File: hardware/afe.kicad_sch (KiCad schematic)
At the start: 27 parts, among them U2 MCP6002-xMC, U3 4052

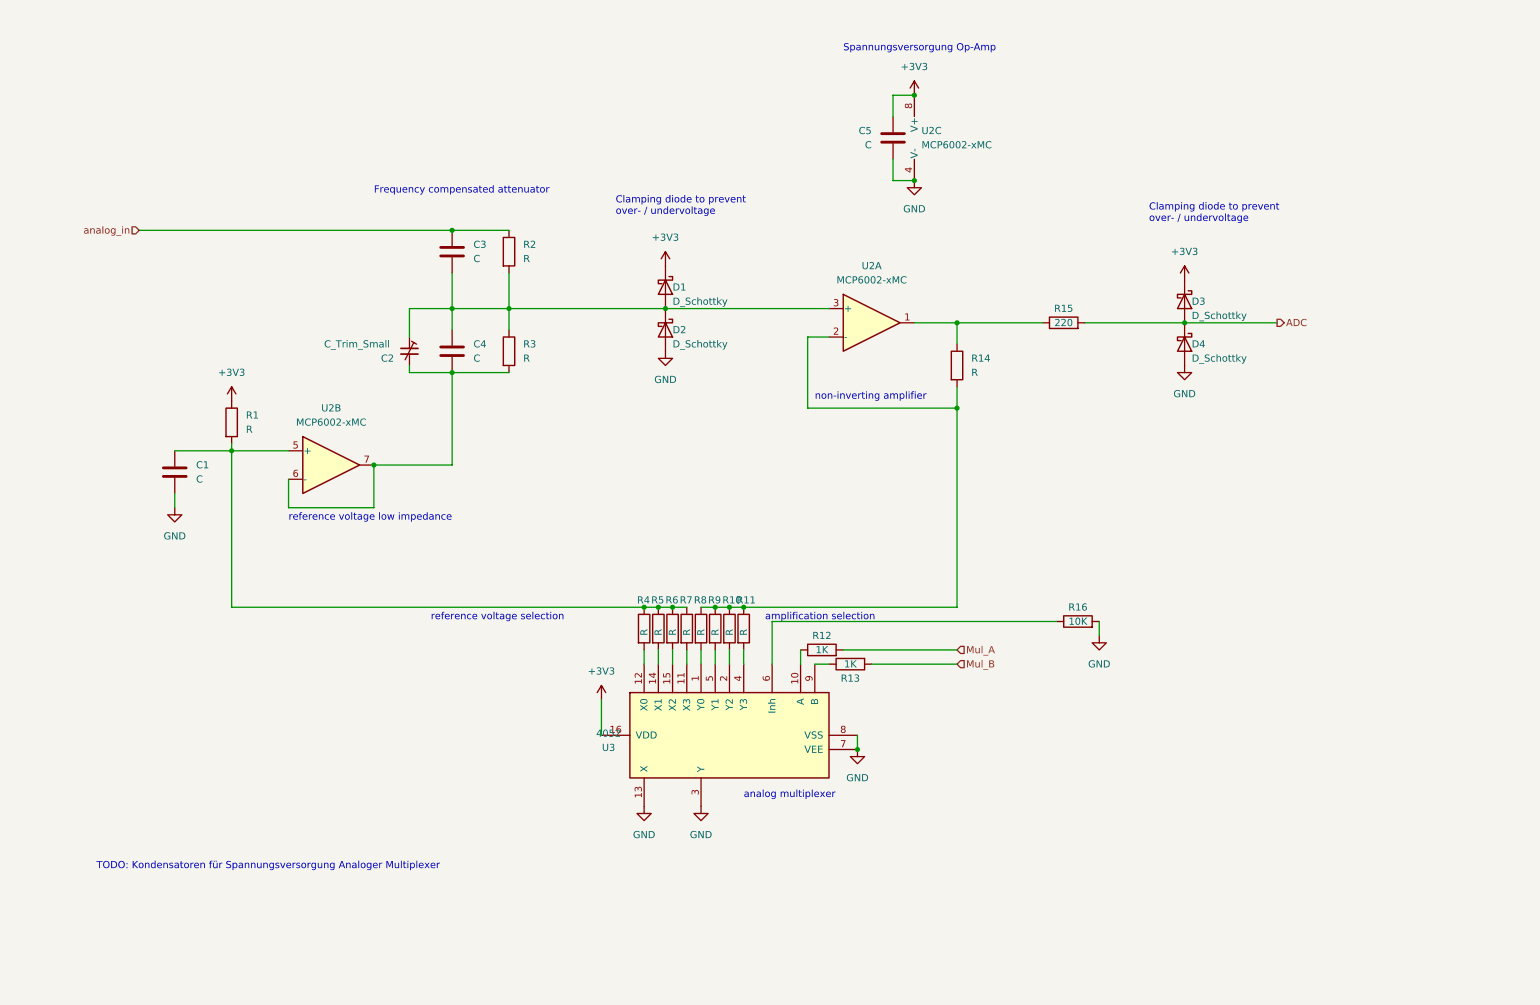
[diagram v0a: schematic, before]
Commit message: started adding some footprints
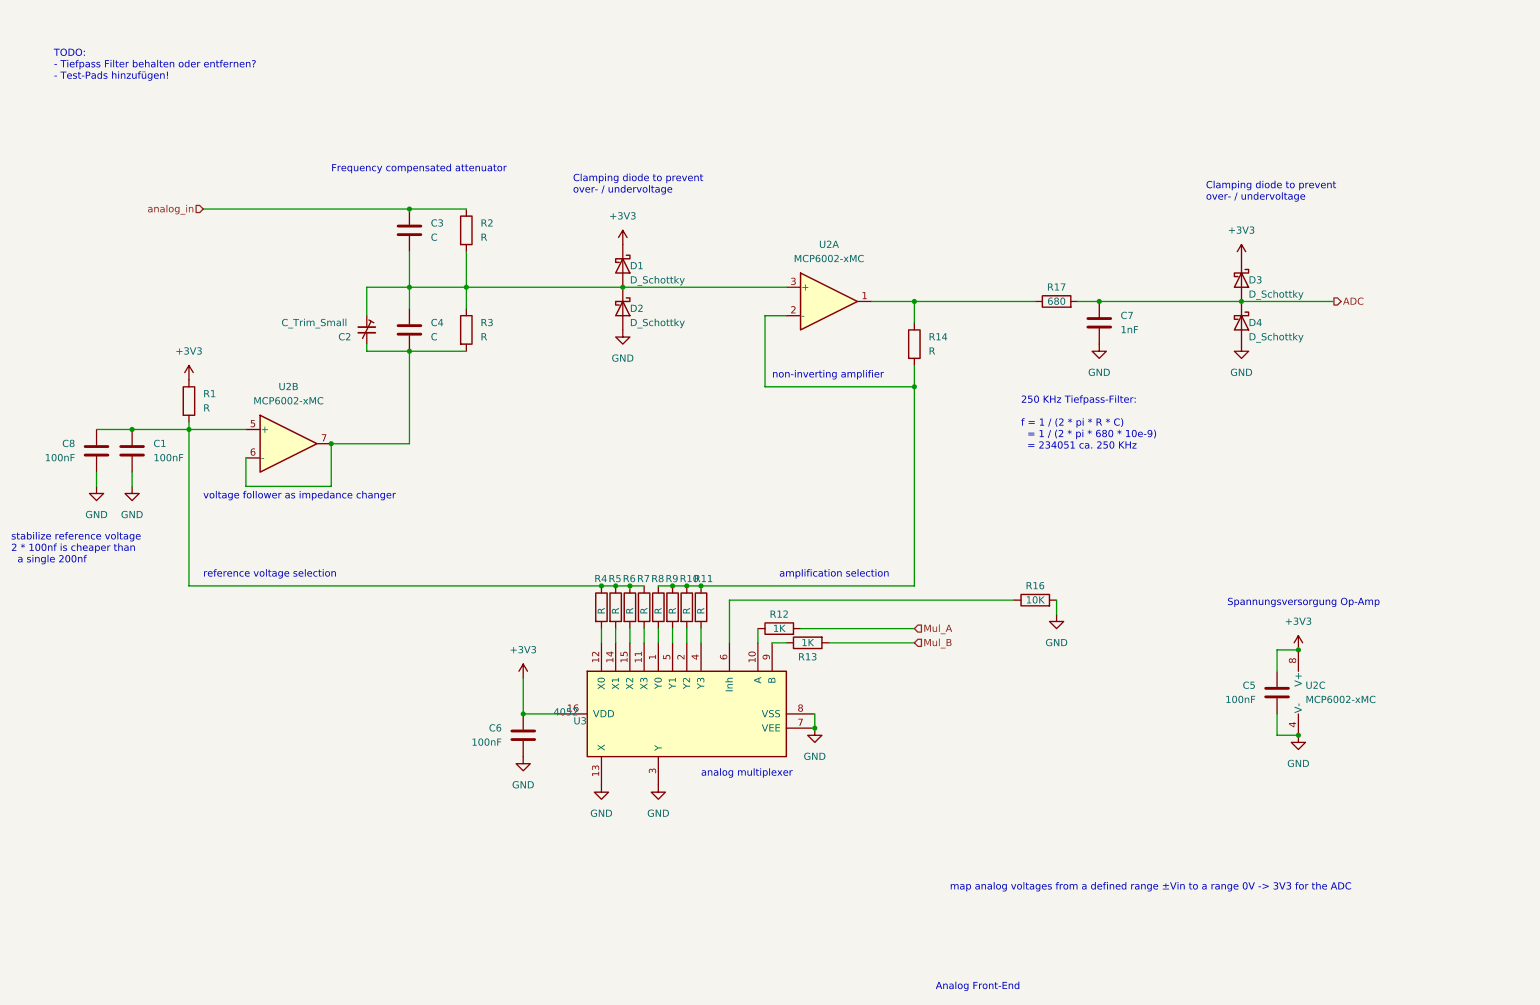
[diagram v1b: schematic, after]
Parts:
- removed R15: 220, symbol Device:R
- added C6, C8: 100nF, Capacitor_SMD:C_0805_2012Metric_Pad1.18x1.45mm_HandSolder, symbol Device:C
- added C7: 1nF, Capacitor_SMD:C_0805_2012Metric_Pad1.18x1.45mm_HandSolder, symbol Device:C
- added R17: 680, Resistor_SMD:R_0805_2012Metric_Pad1.20x1.40mm_HandSolder, symbol Device:R
- C1, C5: value C -> 100nF; footprint (none) -> Capacitor_SMD:C_0805_2012Metric_Pad1.18x1.45mm_HandSolder
- C2: footprint (none) -> additional_parts:c_trim_D5.08mm_P5.08mm
- C3, C4: footprint (none) -> Capacitor_SMD:C_0805_2012Metric_Pad1.18x1.45mm_HandSolder
- R1, R10, R11, R12, R13, R14, R16, R2, R3, R4, R5, R6, R7, R8, R9: footprint (none) -> Resistor_SMD:R_0805_2012Metric_Pad1.20x1.40mm_HandSolder
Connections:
- net +3V3: now also C6.1
- net ADC: now also C7.1, R17.2
- net GND: now also C6.2, C7.2, C8.2
- net at C1.1, R1.2, R4.1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: now also C8.1
- net at R14.1, U2.1: now also R17.1
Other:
- note added: "250 KHz Tiefpass-Filter: f = 1 / (2 * pi * R * C) = 1 / (2 * pi * 680 * 10e-9) = 234051 ca. 250 KHz"
- note added: "Analog Front-End"
- note added: "TODO: - Tiefpass Filter behalten oder entfernen? - Test-Pads hinzufügen!"
- note added: "map analog voltages from a defined range ±Vin to a range 0V -> 3V3 for the ADC"
- note added: "stabilize reference voltage 2 * 100nf is cheaper than a single 200nf"
- note added: "voltage follower as impedance changer"
- note removed: "TODO: Kondensatoren für Spannungsversorgung Analoger Multiplexer"
- note removed: "reference voltage low impedance"
- moved on the sheet: C1, C2, C3, C4, C5, D1, D2, D3, D4, R1, R10, R11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

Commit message: [hard] footprint assignment and some Part Ordering numbers
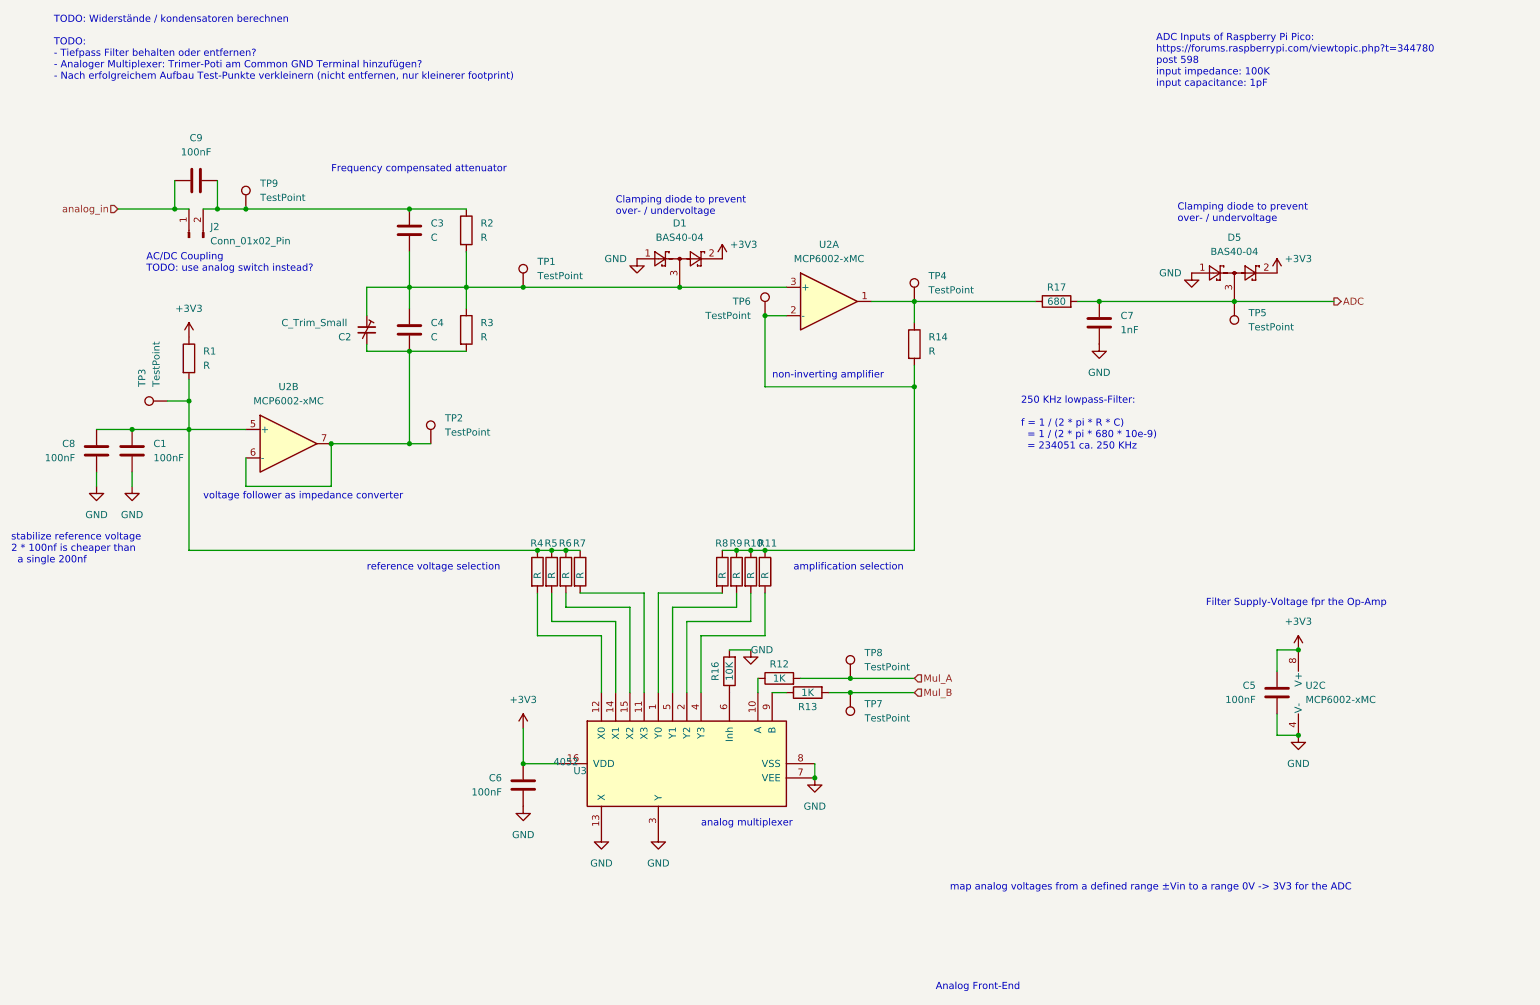
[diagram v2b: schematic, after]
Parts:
- removed D1, D2, D3, D4: D_Schottky, symbol Device:D_Schottky
- added C9: 100nF, Capacitor_SMD:C_0805_2012Metric_Pad1.18x1.45mm_HandSolder, symbol Device:C
- added D1, D5: BAS40-04, Package_TO_SOT_SMD:SOT-23, symbol Diode:BAS40-04
- added J2: Conn_01x02_Pin, Connector_PinHeader_2.54mm:PinHeader_1x02_P2.54mm_Vertical, symbol Connector:Conn_01x02_Pin
- added TP1, TP2, TP3, TP4, TP5, TP6, TP7, TP8, TP9: TestPoint, TestPoint:TestPoint_Pad_D1.5mm, symbol Connector:TestPoint
- U2: Reichelt Part-Number (none) -> MCP 6002-I/SN
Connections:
- net +3V3: now also D1.2, D5.2
- net ADC: now also D5.3, TP5.1
- net GND: now also D1.1, D5.1
- net Mul_A: now also TP8.1
- net Mul_B: now also TP7.1
- net analog_in: now also C9.1, J2.1 (Pin_1); no longer C3.1, R2.1
- net at C1.1, C8.1, R1.2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: now also TP3.1
- net at C2.2, C4.2, R3.2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: now also TP2.1
- net at C2.1, C3.2, C4.1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: now also D1.3, TP1.1
- net at R10.1, R11.1, R14.2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: now also TP6.1
- net at R14.1, R17.1, U2.1: now also TP4.1
- new net: C3.1, C9.2, J2.2 (Pin_2), R2.1, TP9.1
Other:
- note added: "250 KHz lowpass-Filter: f = 1 / (2 * pi * R * C) = 1 / (2 * pi * 680 * 10e-9) = 234051 ca. 250 KHz"
- note added: "AC/DC Coupling TODO: use analog switch instead?"
- note added: "ADC Inputs of Raspberry Pi Pico: https://forums.raspberrypi.com/viewtopic.php?t=344780 post 598 input impedance: 100K input capacitance: 1pF"
- note added: "Filter Supply-Voltage fpr the Op-Amp"
- note added: "TODO: - Tiefpass Filter behalten oder entfernen? - Analoger Multiplexer: Trimer-Poti am Common GND Terminal hinzufügen? - Nach erfolgreichem Aufbau Test-Punkte verkleinern (nicht entfernen, nur kleinerer footprint)"
- note added: "TODO: Widerstände / kondensatoren berechnen"
- note added: "voltage follower as impedance converter"
- note removed: "250 KHz Tiefpass-Filter: f = 1 / (2 * pi * R * C) = 1 / (2 * pi * 680 * 10e-9) = 234051 ca. 250 KHz"
- note removed: "Spannungsversorgung Op-Amp"
- note removed: "TODO: - Tiefpass Filter behalten oder entfernen? - Test-Pads hinzufügen!"
- note removed: "voltage follower as impedance changer"
- moved on the sheet: C6, R1, R10, R11, R12, R13, R16, R4, R5, R6, R7, R8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

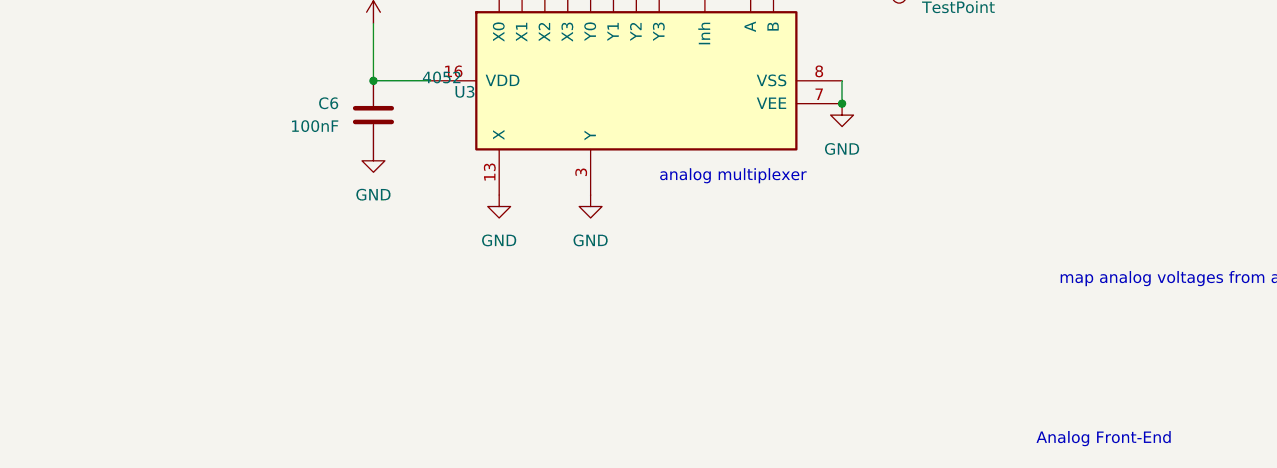
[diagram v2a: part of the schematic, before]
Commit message: [awg] docs and schematics finished but integration not available
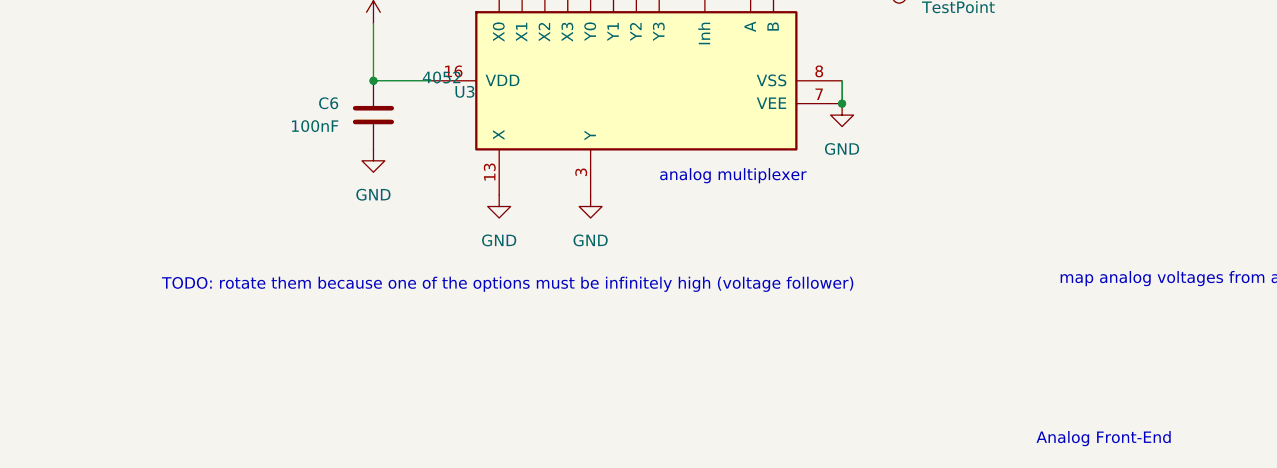
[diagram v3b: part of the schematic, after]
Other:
- note added: "TODO: rotate them because one of the options must be infinitely high (voltage follower)"
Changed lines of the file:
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@@
+    (effects (font (size 1.27 1.27)) (justify left bottom))
+  )
+  (text "TODO: rotate them because one of the options must be infinitely high (voltage follower)"
+    (at 89.535 173.355 0)
     (effects (font (size 1.27 1.27)) (justify left bottom))
   )
